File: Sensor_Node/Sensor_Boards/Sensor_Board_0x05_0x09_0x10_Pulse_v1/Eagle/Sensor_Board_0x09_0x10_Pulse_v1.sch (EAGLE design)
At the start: 20 parts, among them J3 1x3 RA Female .1", J4 ARDUINO_ISP, J6 1x3 RA Female .1", U2 ATMEGA328P_TQFP, Y1 8MHZ

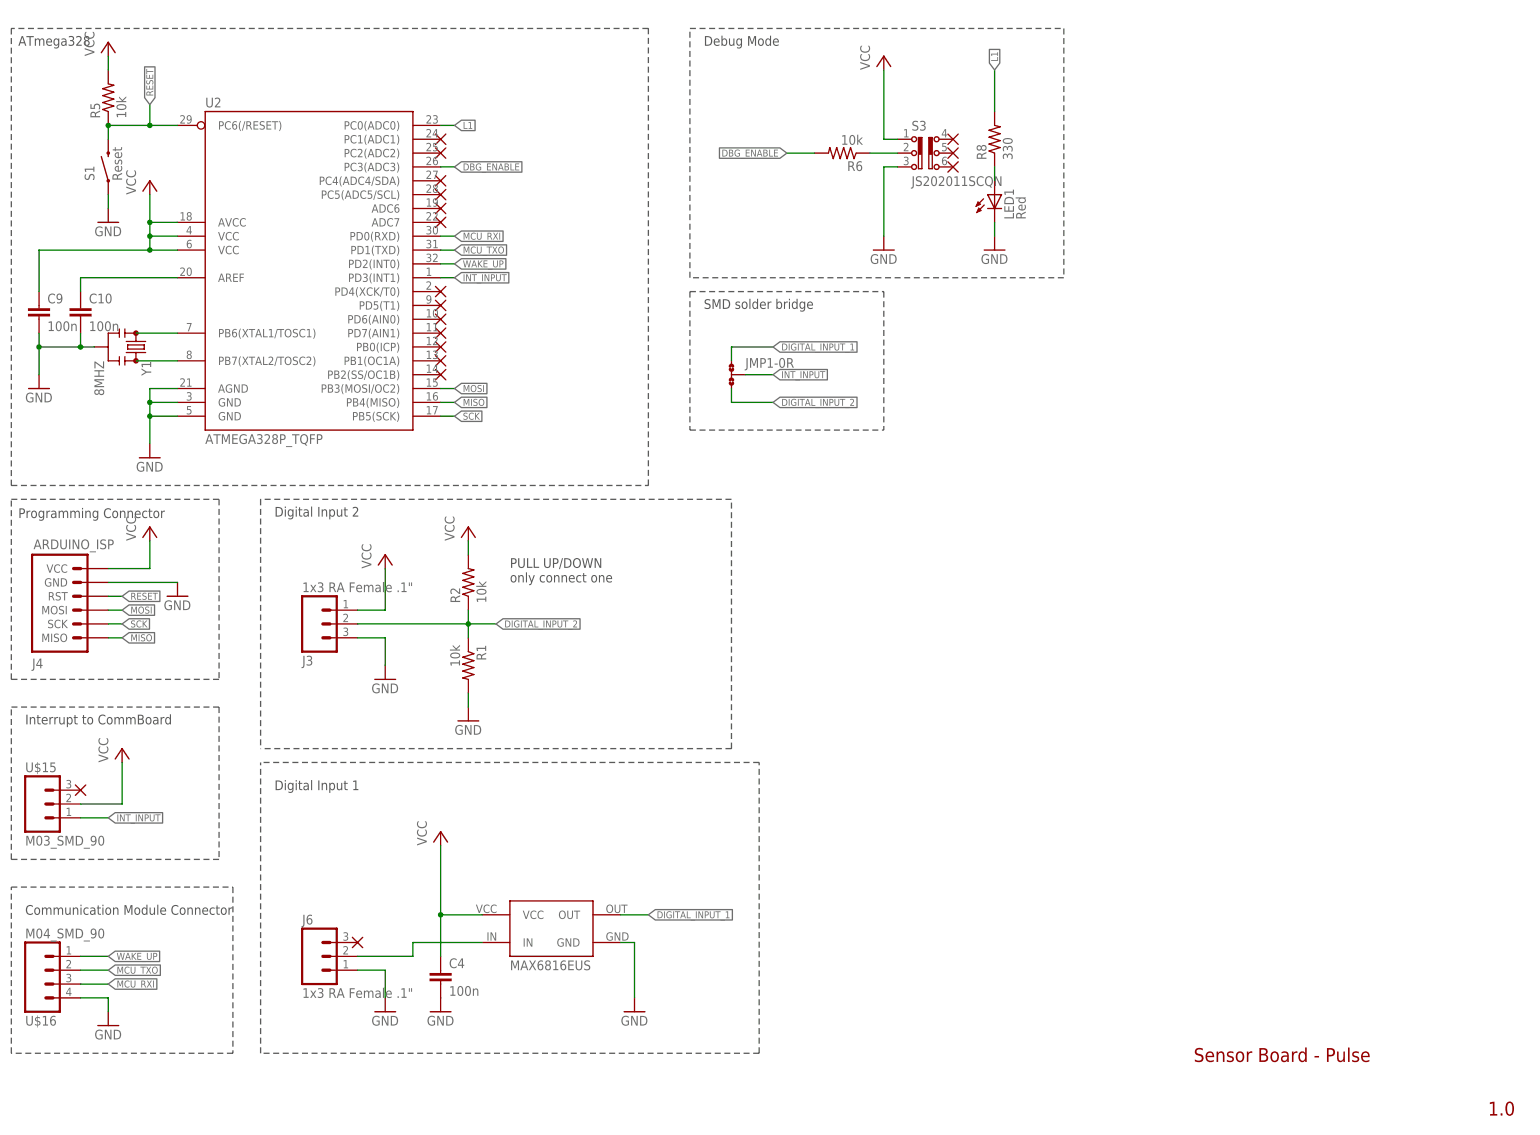
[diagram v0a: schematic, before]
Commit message: Changes on SensModule Pulse
- moved connectors closer together
- turned various components
- added pogopin programming connector
- removed digital input jumper and put digi_input 1 and 2 directly to
PD2, PD3
- put wakeup on PC1
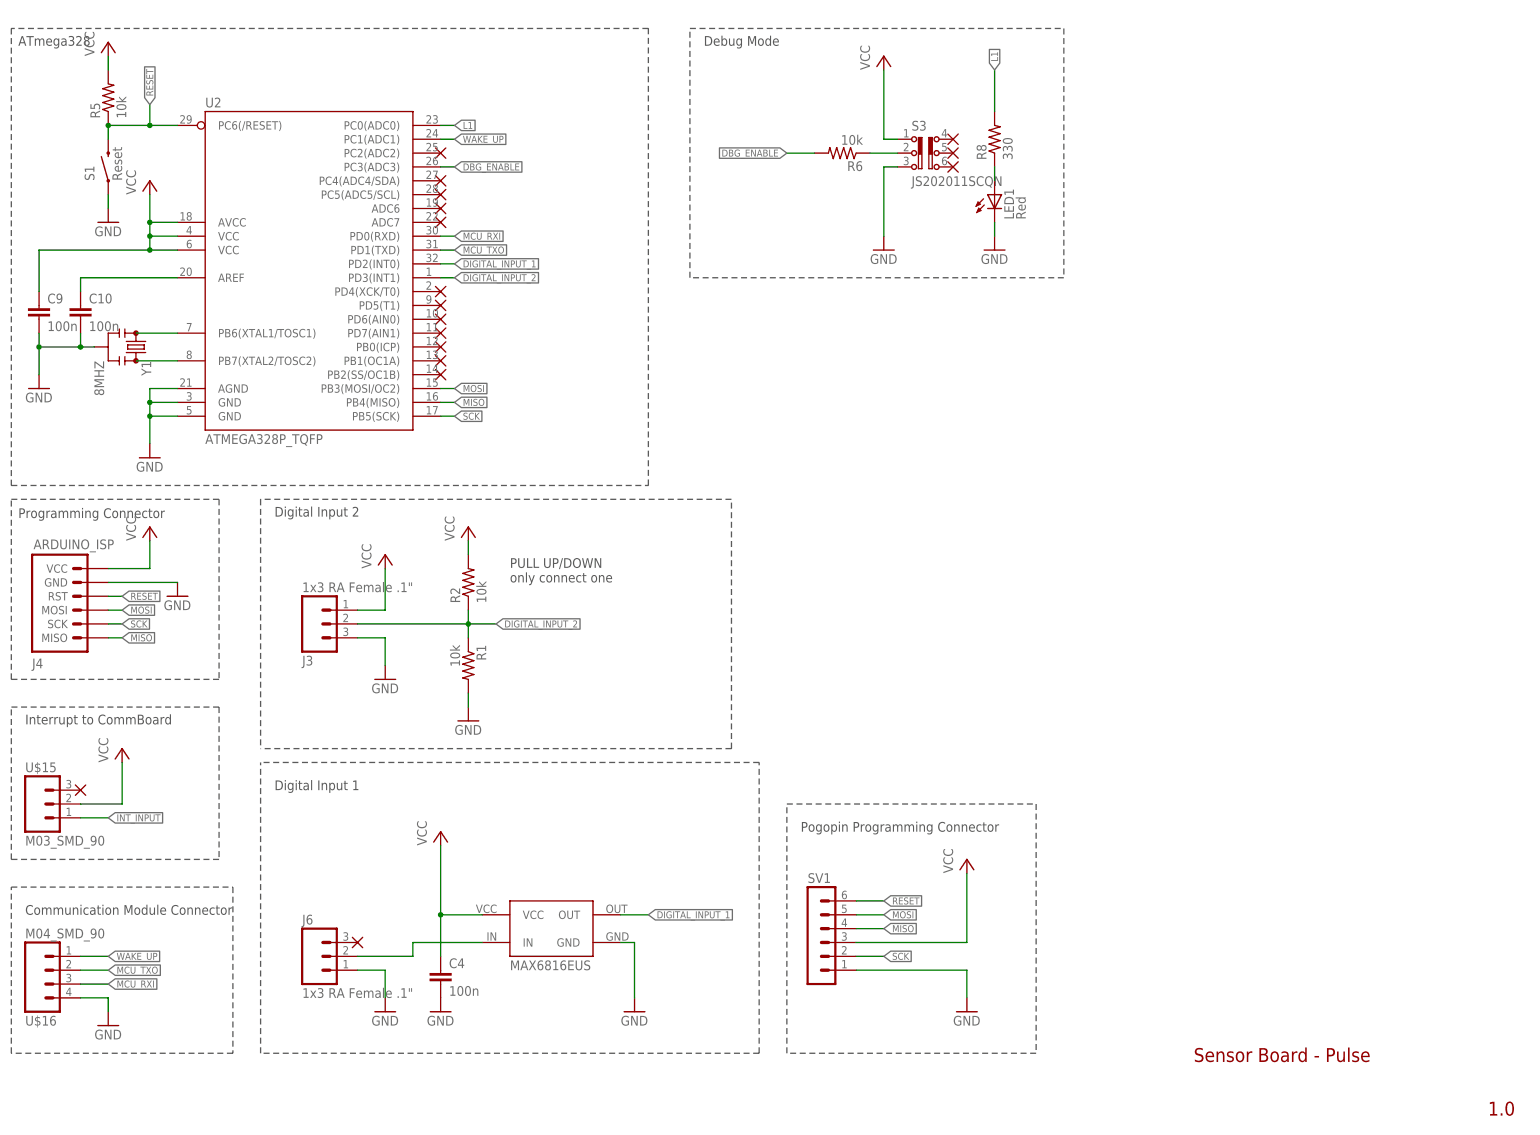
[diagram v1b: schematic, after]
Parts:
- removed JMP1: 0R-JUMPC, jump-0r-smd:0R-JUMPC
- added SV1: (no value), con-lstb:MA06-1
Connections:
- net DIGITAL_INPUT_1: now also U2.PD2(INT0); no longer JMP1-0R.1
- net DIGITAL_INPUT_2: now also U2.PD3(INT1); no longer JMP1-0R.3
- net GND: now also SV1.1
- net INT_INPUT: no longer JMP1-0R.2, U2.PD3(INT1)
- net MISO: now also SV1.4
- net MOSI: now also SV1.5
- net RESET: now also SV1.6
- net SCK: now also SV1.2
- net VCC: now also SV1.3
- net WAKE_UP: now also U2.PC1(ADC1); no longer U2.PD2(INT0)
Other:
- note added: "Pogopin Programming Connector"
- note removed: "SMD solder bridge"
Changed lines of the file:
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@@
 <layers>
 <layer number="1" name="Top" color="4" fill="1" visible="no" active="no"/>
+<layer number="2" name="Route2" color="1" fill="3" visible="no" active="no"/>
+<layer number="3" name="Route3" color="4" fill="3" visible="no" active="no"/>
+<layer number="4" name="Route4" color="1" fill="4" visible="no" active="no"/>
+<layer number="5" name="Route5" color="4" fill="4" visible="no" active="no"/>
+<layer number="6" name="Route6" color="1" fill="8" visible="no" active="no"/>
+<layer number="7" name="Route7" color="4" fill="8" visible="no" active="no"/>
+<layer number="8" name="Route8" color="1" fill="2" visible="no" active="no"/>
+<layer number="9" name="Route9" color="4" fill="2" visible="no" active="no"/>
+<layer number="10" name="Route10" color="1" fill="7" visible="no" active="no"/>
+<layer number="11" name="Route11" color="4" fill="7" visible="no" active="no"/>
+<layer number="12" name="Route12" color="1" fill="5" visible="no" active="no"/>
+<layer number="13" name="Route13" color="4" fill="5" visible="no" active="no"/>
+<layer number="14" name="Route14" color="1" fill="6" visible="no" active="no"/>
+<layer number="15" name="Route15" color="4" fill="6" visible="no" active="no"/>
 <layer number="16" name="Bottom" color="1" fill="1" visible="no" active="no"/>
 <layer number="17" name="Pads" color="2" fill="1" visible="no" active="no"/>
@@
 <part name="GND1" library="SparkFun" deviceset="GND" device=""/>
 <part name="J3" library="SparkFun-Connectors" deviceset="M03" device="SMD_RA_FEMALE" value="1x3 RA Female .1&quot;"/>
-<part name="JMP1" library="jump-0r-smd" deviceset="0R-JUMP" device="C"/>
 <part name="R1" library="SparkFun-Passives" deviceset="RESISTOR" device="0805-RES" value="10k"/>
 <part name="R2" library="SparkFun-Passives" deviceset="RESISTOR" device="0805-RES" value="10k"/>
@@
 <part name="U$15" library="myownthings" deviceset="M03_SMD_90" device=""/>
 <part name="U$16" library="myownthings" deviceset="M04_SMD_90" device=""/>
-<part name="U$17" library="myownthings" deviceset="N/C" device=""/>
 <part name="U$18" library="myownthings" deviceset="N/C" device=""/>
 <part name="U$19" library="myownthings" deviceset="N/C" device=""/>
 <part name="U$20" library="myownthings" deviceset="N/C" device=""/>
 <part name="U$21" library="myownthings" deviceset="N/C" device=""/>
+<part name="SV1" library="con-lstb" deviceset="MA06-1" device=""/>
+<part name="P+9" library="supply1" deviceset="VCC" device=""/>
+<part name="GND6" library="SparkFun" deviceset="GND" device=""/>
 </parts>
 <sheets>
@@
 <wire x1="45.72" y1="48.26" x2="7.62" y2="48.26" width="0.1524" layer="97" style="shortdash"/>
 <wire x1="45.72" y1="76.2" x2="45.72" y2="48.26" width="0.1524" layer="97" style="shortdash"/>
-<wire x1="132.08" y1="127" x2="167.64" y2="127" width="0.1524" layer="97" style="shortdash"/>
 <wire x1="139.7" y1="114.3" x2="53.34" y2="114.3" width="0.1524" layer="97" style="shortdash"/>
-<wire x1="132.08" y1="152.4" x2="132.08" y2="127" width="0.1524" layer="97" style="shortdash"/>
 <wire x1="139.7" y1="68.58" x2="139.7" y2="114.3" width="0.1524" layer="97" style="shortdash"/>
 <wire x1="139.7" y1="68.58" x2="53.34" y2="68.58" width="0.1524" layer="97" style="shortdash"/>
-<wire x1="132.08" y1="152.4" x2="167.64" y2="152.4" width="0.1524" layer="97" style="shortdash"/>
 <wire x1="53.34" y1="114.3" x2="53.34" y2="68.58" width="0.1524" layer="97" style="shortdash"/>
-<wire x1="167.64" y1="152.4" x2="167.64" y2="127" width="0.1524" layer="97" style="shortdash"/>
 <text x="55.88" y="111.125" size="1.778" layer="97">Digital Input 2</text>
-<text x="134.62" y="149.225" size="1.778" layer="97">SMD solder bridge</text>
 <text x="10.16" y="73.025" size="1.778" layer="97">Interrupt to CommBoard</text>
 <text x="99.06" y="99.06" size="1.778" layer="97">PULL UP/DOWN
@@
 <text x="278.4475" y="1.27" size="2.54" layer="94" font="vector">1.0</text>
 <text x="224.4725" y="11.1125" size="2.54" layer="94" font="vector">Sensor Board - Pulse</text>
+<wire x1="149.86" y1="58.42" x2="195.58" y2="58.42" width="0.1524" layer="97" style="shortdash"/>
+<wire x1="195.58" y1="58.42" x2="195.58" y2="12.7" width="0.1524" layer="97" style="shortdash"/>
+<wire x1="195.58" y1="12.7" x2="149.86" y2="12.7" width="0.1524" layer="97" style="shortdash"/>
+<wire x1="149.86" y1="12.7" x2="149.86" y2="58.42" width="0.1524" layer="97" style="shortdash"/>
+<text x="152.4" y="53.34" size="1.778" layer="97">Pogopin Programming Connector</text>
 </plain>
 <instances>
@@
 <instance part="GND1" gate="1" x="76.2" y="81.28"/>
 <instance part="J3" gate="J$1" x="63.5" y="91.44" rot="MR180"/>
-<instance part="JMP1" gate="-0R" x="139.7" y="137.16"/>
 <instance part="R1" gate="G$1" x="91.44" y="83.82" rot="R270"/>
 <instance part="R2" gate="G$1" x="91.44" y="99.06" rot="R90"/>
@@
 <instance part="U$15" gate="G$1" x="12.7" y="58.42"/>
 <instance part="U$16" gate="G$1" x="15.24" y="27.94" rot="MR180"/>
-<instance part="U$17" gate="G$1" x="86.36" y="180.34"/>
 <instance part="U$18" gate="G$1" x="86.36" y="177.8"/>
 <instance part="U$19" gate="G$1" x="180.34" y="180.34"/>
 <instance part="U$20" gate="G$1" x="180.34" y="177.8"/>
 <instance part="U$21" gate="G$1" x="180.34" y="175.26"/>
+<instance part="SV1" gate="1" x="154.94" y="35.56"/>
+<instance part="P+9" gate="VCC" x="182.88" y="48.26"/>
+<instance part="GND6" gate="1" x="182.88" y="20.32"/>
 </instances>
 <busses>
@@
 <pinref part="GND3" gate="1" pin="GND"/>
 <wire x1="91.44" y1="78.74" x2="91.44" y2="76.2" width="0.1524" layer="91"/>
+</segment>
+<segment>
+<pinref part="GND6" gate="1" pin="GND"/>
+<wire x1="182.88" y1="22.86" x2="182.88" y2="27.94" width="0.1524" layer="91"/>
+<pinref part="SV1" gate="1" pin="1"/>
+<wire x1="182.88" y1="27.94" x2="162.56" y2="27.94" width="0.1524" layer="91"/>
 </segment>
 </net>
@@
 <wire x1="167.64" y1="180.34" x2="170.18" y2="180.34" width="0.1524" layer="91"/>
 </segment>
+<segment>
+<pinref part="SV1" gate="1" pin="3"/>
+<pinref part="P+9" gate="VCC" pin="VCC"/>
+<wire x1="162.56" y1="33.02" x2="182.88" y2="33.02" width="0.1524" layer="91"/>
+<wire x1="182.88" y1="33.02" x2="182.88" y2="45.72" width="0.1524" layer="91"/>
+</segment>
 </net>
 <net name="RESET" class="0">
@@
 <pinref part="J4" gate="G$1" pin="RST"/>
 </segment>
+<segment>
+<pinref part="SV1" gate="1" pin="6"/>
+<wire x1="162.56" y1="40.64" x2="167.64" y2="40.64" width="0.1524" layer="91"/>
+<label x="167.64" y="40.64" size="1.27" layer="95" xref="yes"/>
+</segment>
 </net>
 <net name="SCK" class="0">
@@
 <pinref part="U2" gate="U$1" pin="PB5(SCK)"/>
 </segment>
+<segment>
+<pinref part="SV1" gate="1" pin="2"/>
+<wire x1="162.56" y1="30.48" x2="167.64" y2="30.48" width="0.1524" layer="91"/>
+<label x="167.64" y="30.48" size="1.27" layer="95" xref="yes"/>
+</segment>
 </net>
 <net name="MISO" class="0">
@@
 <pinref part="U2" gate="U$1" pin="PB4(MISO)"/>
 </segment>
+<segment>
+<pinref part="SV1" gate="1" pin="4"/>
+<wire x1="162.56" y1="35.56" x2="167.64" y2="35.56" width="0.1524" layer="91"/>
+<label x="167.64" y="35.56" size="1.27" layer="95" xref="yes"/>
+</segment>
 </net>
 <net name="MOSI" class="0">
@@
 <label x="88.9" y="134.62" size="1.27" layer="95" xref="yes"/>
 <pinref part="U2" gate="U$1" pin="PB3(MOSI/OC2)"/>
+</segment>
+<segment>
+<pinref part="SV1" gate="1" pin="5"/>
+<wire x1="162.56" y1="38.1" x2="167.64" y2="38.1" width="0.1524" layer="91"/>
+<label x="167.64" y="38.1" size="1.27" layer="95" xref="yes"/>
 </segment>
 </net>
@@
 </segment>
 <segment>
-<pinref part="U2" gate="U$1" pin="PD2(INT0)"/>
-<wire x1="86.36" y1="157.48" x2="88.9" y2="157.48" width="0.1524" layer="91"/>
-<label x="88.9" y="157.48" size="1.27" layer="95" xref="yes"/>
+<pinref part="U2" gate="U$1" pin="PC1(ADC1)"/>
+<wire x1="86.36" y1="180.34" x2="88.9" y2="180.34" width="0.1524" layer="91"/>
+<label x="88.9" y="180.34" size="1.27" layer="95" xref="yes"/>
 </segment>
 </net>
 <net name="DIGITAL_INPUT_2" class="0">
-<segment>
-<pinref part="JMP1" gate="-0R" pin="3"/>
-<wire x1="139.7" y1="134.62" x2="139.7" y2="132.08" width="0.1524" layer="91"/>
-<wire x1="139.7" y1="132.08" x2="147.32" y2="132.08" width="0.1524" layer="91"/>
-<label x="147.32" y="132.08" size="1.27" layer="95" xref="yes"/>
-</segment>
 <segment>
 <pinref part="J3" gate="J$1" pin="2"/>
@@
 <label x="96.52" y="91.44" size="1.27" layer="95" xref="yes"/>
 </segment>
-</net>
-<net name="INT_INPUT" class="0">
 <segment>
 <pinref part="U2" gate="U$1" pin="PD3(INT1)"/>
@@
 <label x="88.9" y="154.94" size="1.27" layer="95" xref="yes"/>
 </segment>
-<segment>
-<pinref part="JMP1" gate="-0R" pin="2"/>
-<wire x1="142.24" y1="137.16" x2="147.32" y2="137.16" width="0.1524" layer="91"/>
-<label x="147.32" y="137.16" size="1.27" layer="95" xref="yes"/>
-</segment>
+</net>
+<net name="INT_INPUT" class="0">
 <segment>
 <pinref part="U$15" gate="G$1" pin="1"/>
@@
 <net name="DIGITAL_INPUT_1" class="0">
 <segment>
-<pinref part="JMP1" gate="-0R" pin="1"/>
-<wire x1="139.7" y1="139.7" x2="139.7" y2="142.24" width="0.1524" layer="91"/>
-<wire x1="139.7" y1="142.24" x2="147.32" y2="142.24" width="0.1524" layer="91"/>
-<label x="147.32" y="142.24" size="1.27" layer="95" xref="yes"/>
-</segment>
-<segment>
 <pinref part="U$2" gate="G$1" pin="OUT"/>
 <wire x1="119.38" y1="38.1" x2="124.46" y2="38.1" width="0.1524" layer="91"/>
 <label x="124.46" y="38.1" size="1.27" layer="95" xref="yes"/>
 </segment>
-</net>
+<segment>
+<pinref part="U2" gate="U$1" pin="PD2(INT0)"/>
+<wire x1="86.36" y1="157.48" x2="88.9" y2="157.48" width="0.1524" layer="91"/>
+<label x="88.9" y="157.48" size="1.27" layer="95" xref="yes"/>
+</segment>
+</net>

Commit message: Changes on all boards
- added capacitor on reset-path
- changed order of pogopin programmer pins

Pulse-Board:
- Deleted input-jumper. Currently one interrupt-pin missing, so print is
not yet routed.
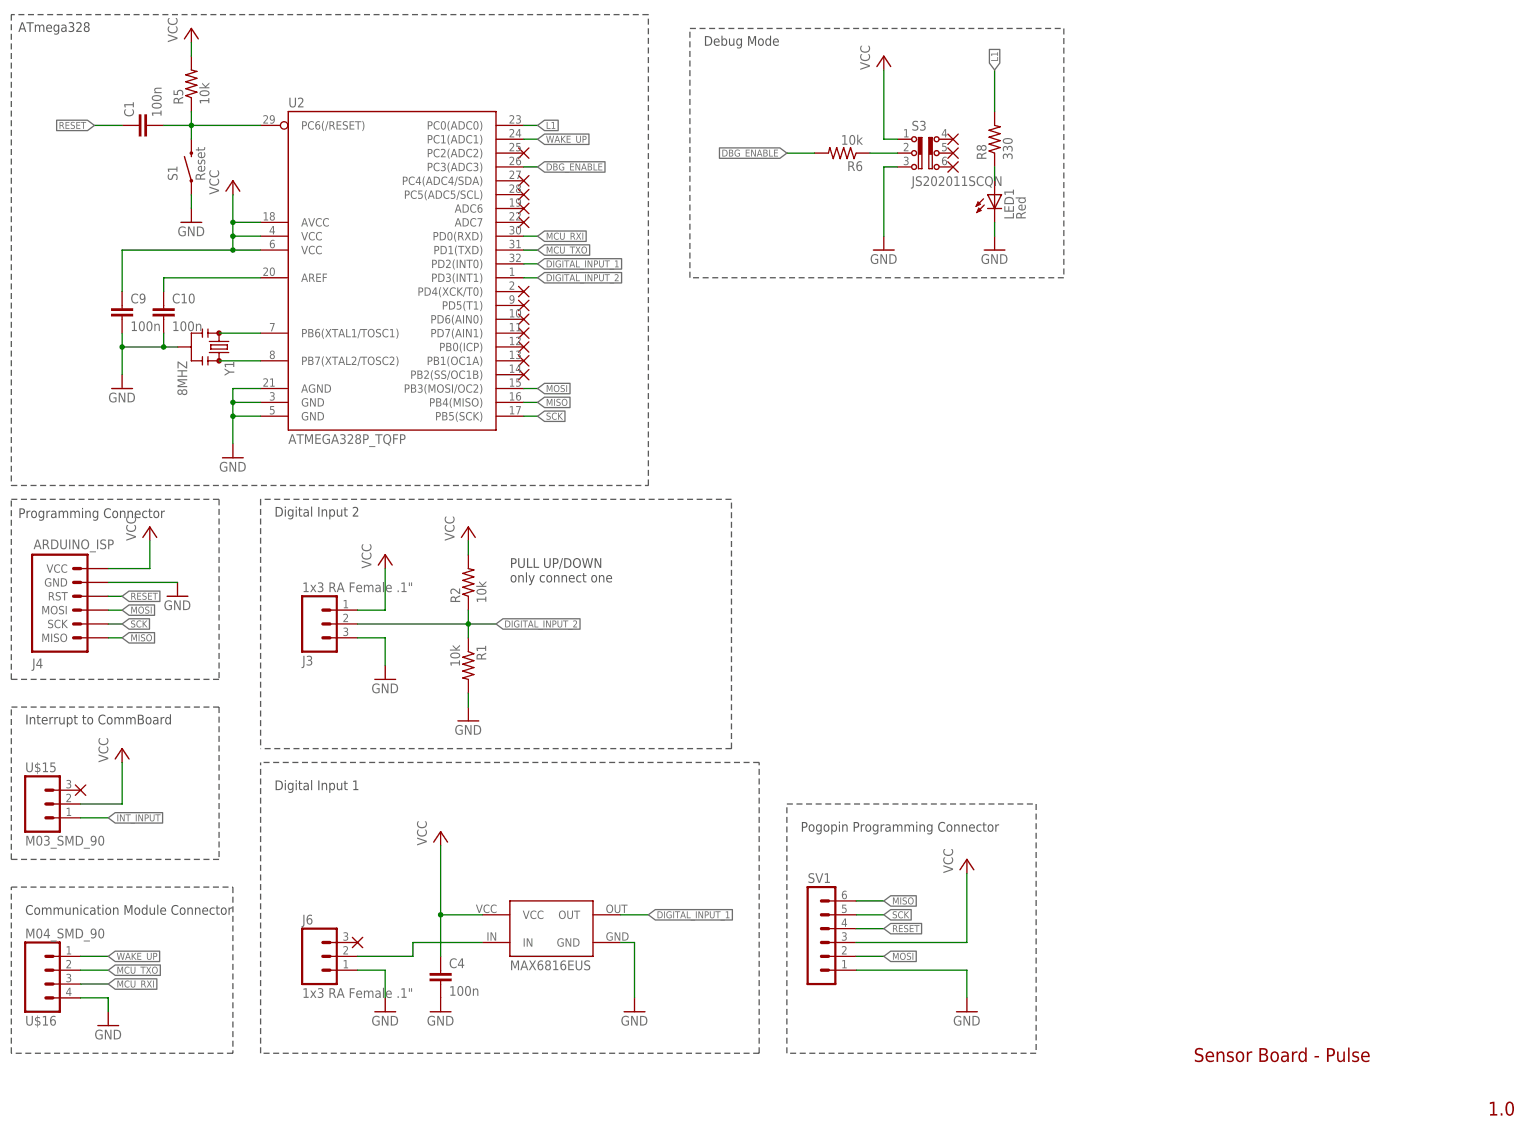
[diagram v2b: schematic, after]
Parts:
- added C1: 100n, eagle-ltspice:C
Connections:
- new net N$5: C1.2, R5.1, S1.RIGHT, U2.PC6(/RESET)
- net MISO: now also SV1.6; no longer SV1.4
- net MOSI: now also SV1.2; no longer SV1.5
- net RESET: now also C1.1, SV1.4; no longer R5.1, S1.RIGHT, SV1.6, U2.PC6(/RESET)
- net SCK: now also SV1.5; no longer SV1.2
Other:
- moved on the sheet: C10, C9, R5, S1, U2, Y1
